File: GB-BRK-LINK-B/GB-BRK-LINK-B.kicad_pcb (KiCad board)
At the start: 2 copper layers, 30 x 35 mm, 6 parts, among them J1 Conn_01x06, J2 GameBoy_LinkPort

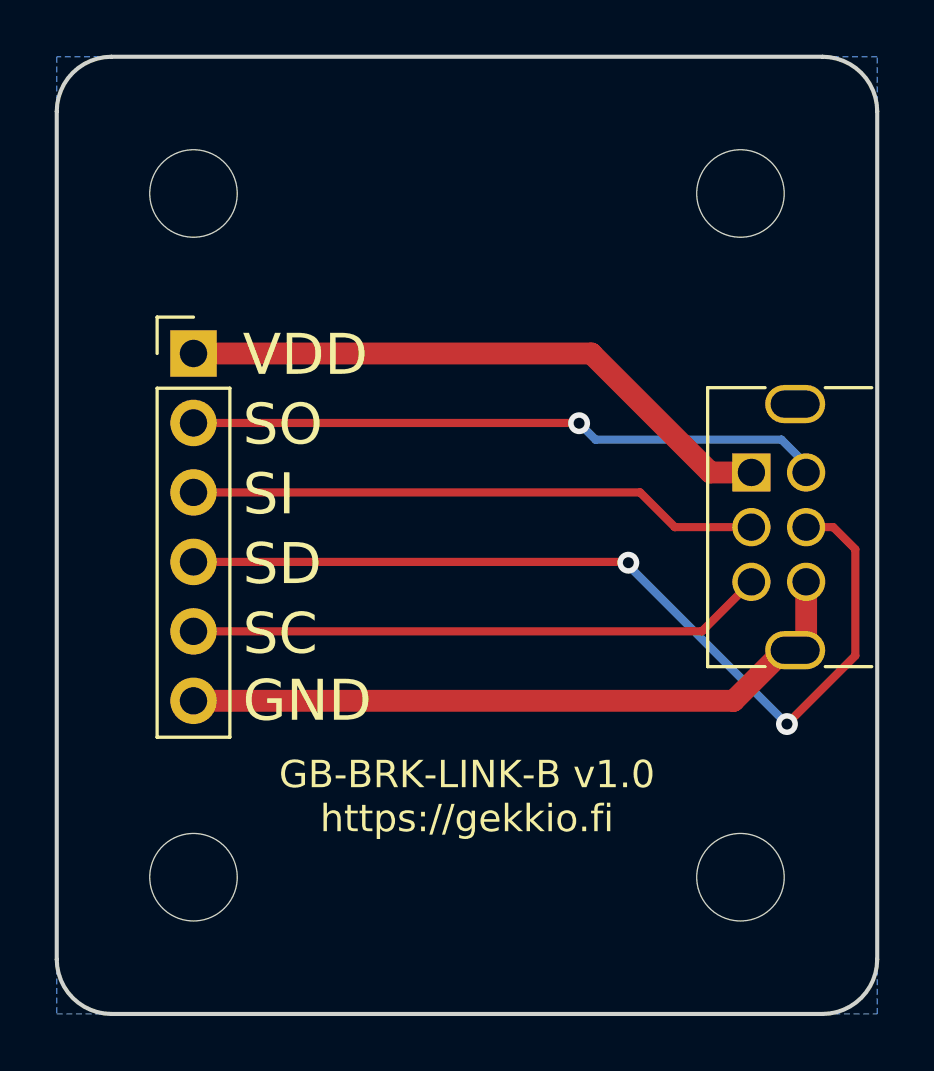
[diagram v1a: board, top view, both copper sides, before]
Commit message: Upgrade most projects to KiCad 6
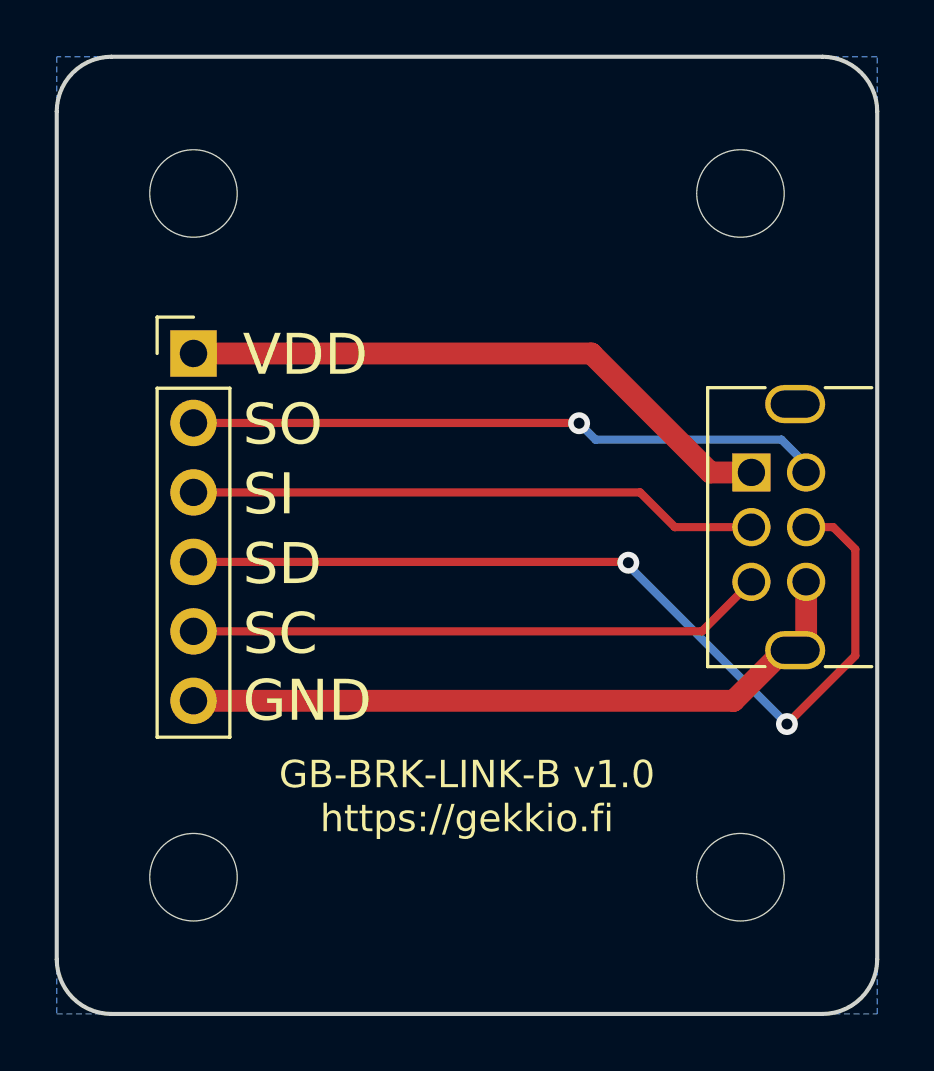
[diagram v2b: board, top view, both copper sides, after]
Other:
- net class Default removed
